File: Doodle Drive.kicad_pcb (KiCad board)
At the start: 2 copper layers, 99.1 x 99.1 mm, 52 parts, among them J1 USB_C_Receptacle, J2 PINHD_1x4_Male, J3 PINHD_1x4_Male, SW1 Push_Button, SW2 Push_Button, SW3 Push_Button, U1 STM32F401CEUx, U2 DRV8825PWP, U6 AP7343-30W5-7, Y1 32.768KHz ±20ppm 12.5pF, Y3 25MHZ 9PF

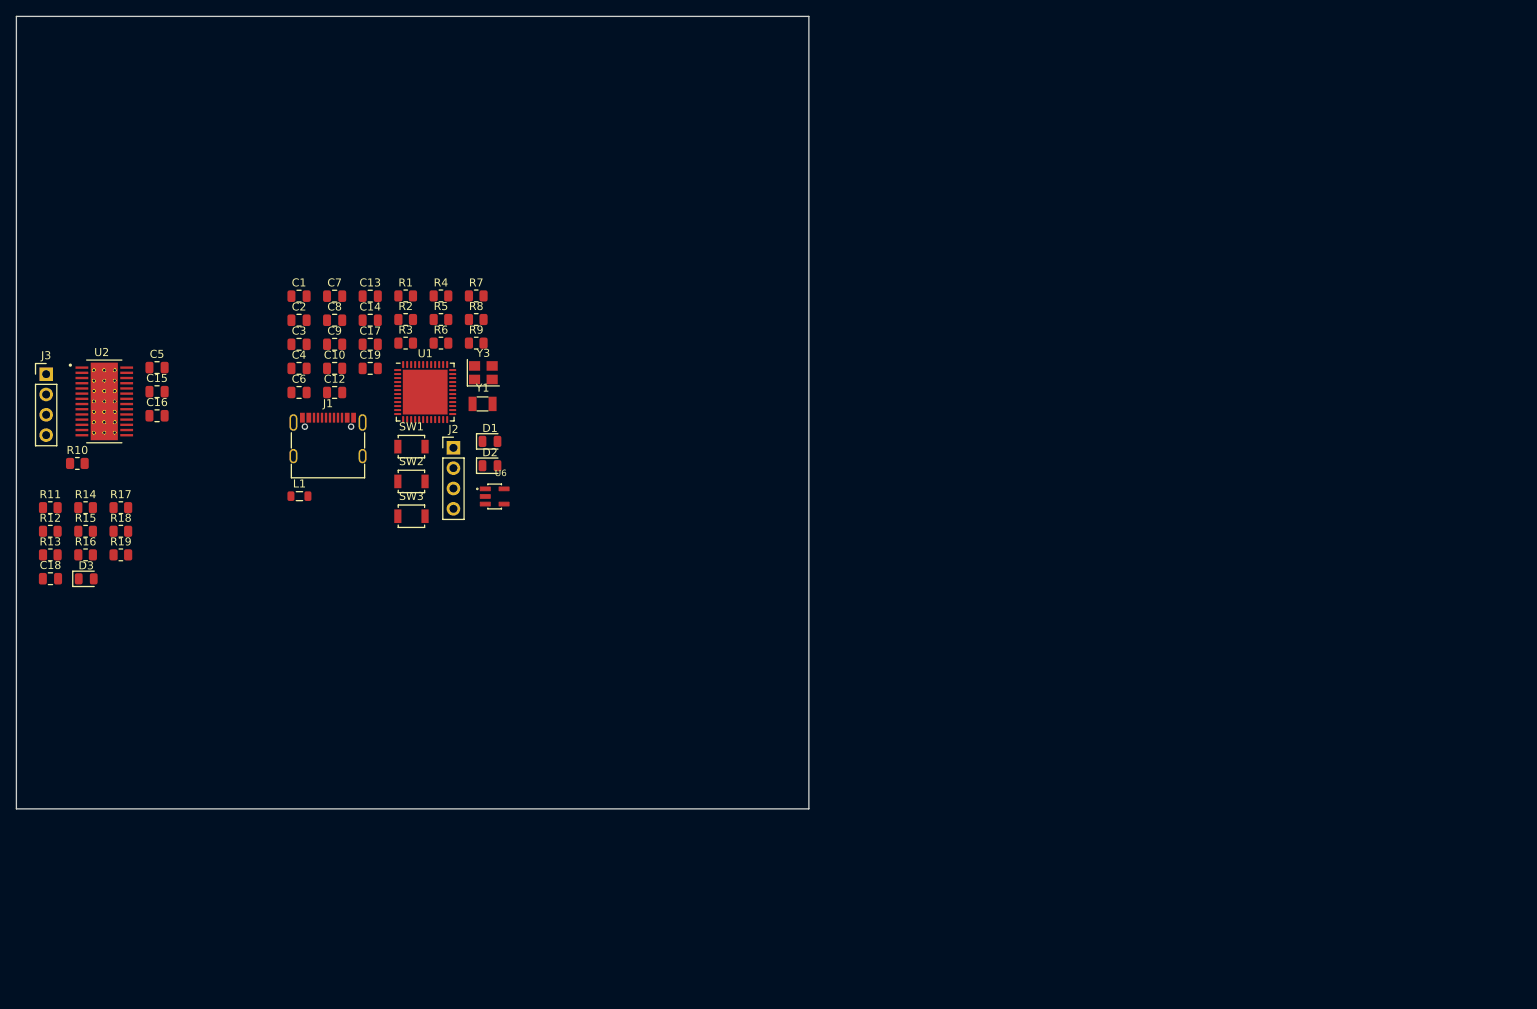
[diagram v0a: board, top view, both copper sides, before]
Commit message: fixed few errors, added test points
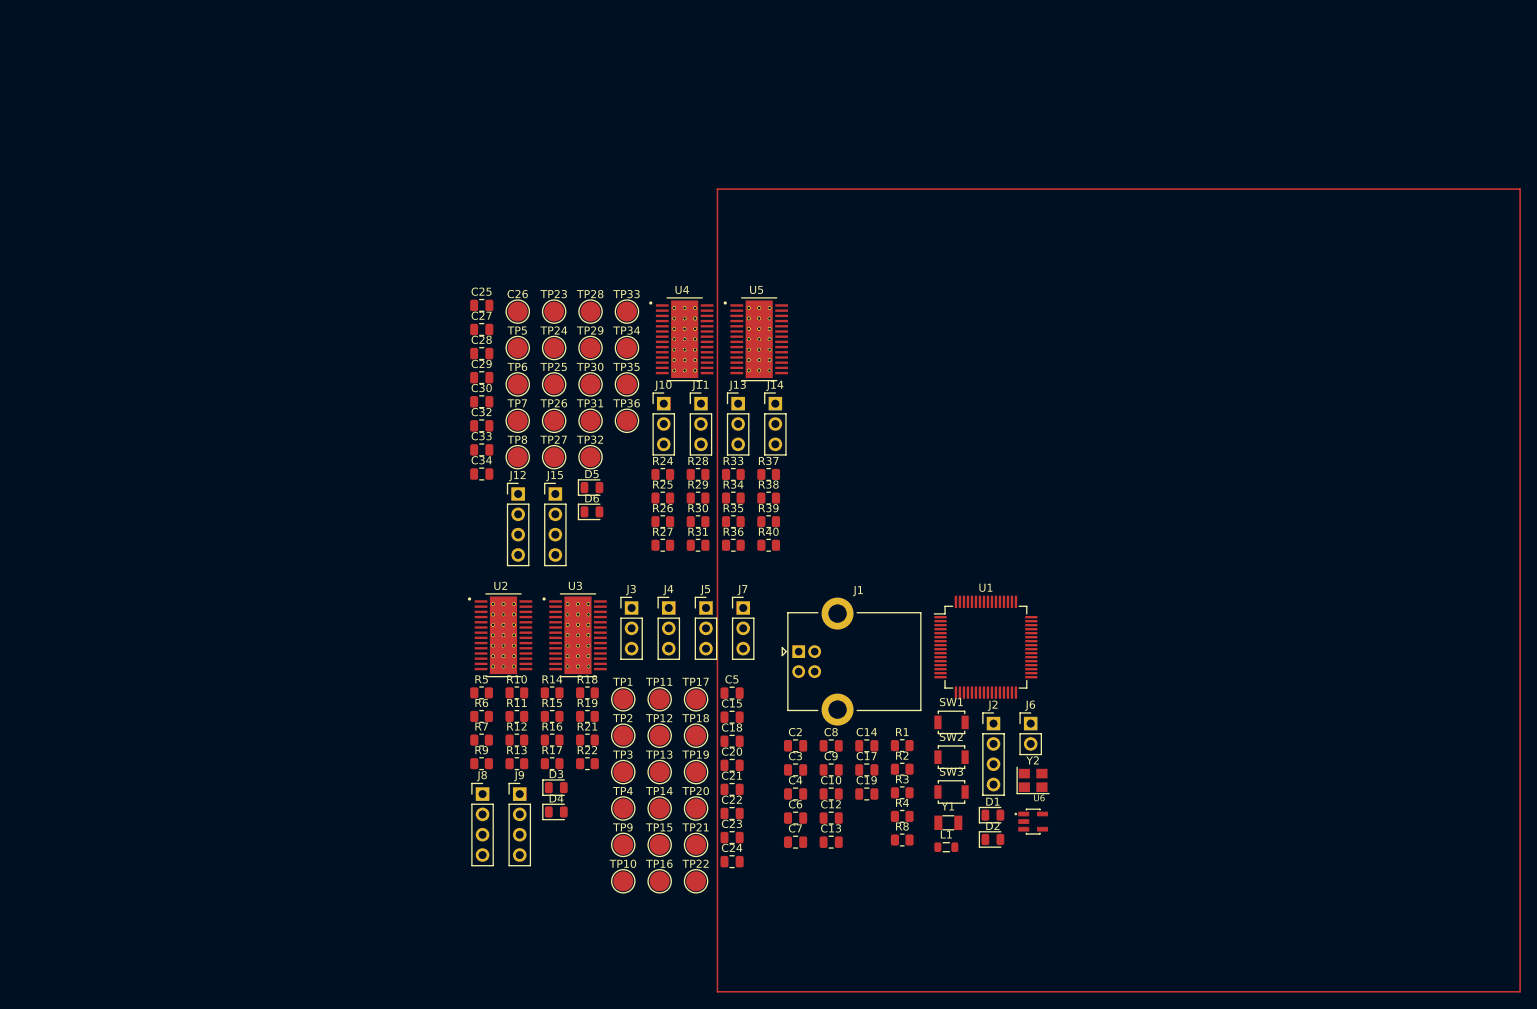
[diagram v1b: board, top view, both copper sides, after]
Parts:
- removed C1: 1uF, Capacitor_SMD:C_0805_2012Metric
- removed C16: Bulk Capacitance. 4.7uF?, Capacitor_SMD:C_0805_2012Metric
- removed Y3: 25MHZ 9PF, Crystal:Crystal_SMD_3225-4Pin_3.2x2.5mm
- added C20: 100nF 50V, Capacitor_SMD:C_0805_2012Metric, F.Cu at (135.2, 127.9)
- added C21: 100nF 50V, Capacitor_SMD:C_0805_2012Metric, F.Cu at (135.2, 130.9)
- added C22: Bulk Capacitance. 4.7uF?, Capacitor_SMD:C_0805_2012Metric, F.Cu at (135.2, 133.9)
- added C23: 100nF 50V, Capacitor_SMD:C_0805_2012Metric, F.Cu at (135.2, 136.9)
- added C24: 100nF 50V, Capacitor_SMD:C_0805_2012Metric, F.Cu at (135.2, 139.9)
- added C25: 10nF 50V, Capacitor_SMD:C_0805_2012Metric, F.Cu at (103.9, 70.4)
- added C26: 100nF 16V ceramic, TestPoint:TestPoint_Pad_D2.5mm, F.Cu at (108.4, 71.2)
- added C27: Bulk Capacitance. 4.7uF?, Capacitor_SMD:C_0805_2012Metric, F.Cu at (103.9, 73.4)
- added C28: 100nF 50V, Capacitor_SMD:C_0805_2012Metric, F.Cu at (103.9, 76.4)
- added C29: 100nF 50V, Capacitor_SMD:C_0805_2012Metric, F.Cu at (103.9, 79.5)
- added C30: 10nF 50V, Capacitor_SMD:C_0805_2012Metric, F.Cu at (103.9, 82.5)
- added C32: Bulk Capacitance. 4.7uF?, Capacitor_SMD:C_0805_2012Metric, F.Cu at (103.9, 85.5)
- added C33: 100nF 50V, Capacitor_SMD:C_0805_2012Metric, F.Cu at (103.9, 88.5)
- added C34: 100nF 50V, Capacitor_SMD:C_0805_2012Metric, F.Cu at (103.9, 91.5)
- added D4: LED_RED, LED_SMD:LED_0805_2012Metric, F.Cu at (113.2, 133.7)
- added D5: LED_RED, LED_SMD:LED_0805_2012Metric, F.Cu at (117.7, 93.2)
- added D6: LED_RED, LED_SMD:LED_0805_2012Metric, F.Cu at (117.7, 96.2)
- added J10: PINHD_1x3_Male, Connector_PinHeader_2.54mm:PinHeader_1x03_P2.54mm_Vertical, F.Cu at (126.6, 82.7)
- added J11: PINHD_1x3_Male, Connector_PinHeader_2.54mm:PinHeader_1x03_P2.54mm_Vertical, F.Cu at (131.3, 82.7)
- added J12: PINHD_1x4_Male, Connector_PinHeader_2.54mm:PinHeader_1x04_P2.54mm_Vertical, F.Cu at (108.4, 94.0)
- added J13: PINHD_1x3_Male, Connector_PinHeader_2.54mm:PinHeader_1x03_P2.54mm_Vertical, F.Cu at (135.9, 82.7)
- added J14: PINHD_1x3_Male, Connector_PinHeader_2.54mm:PinHeader_1x03_P2.54mm_Vertical, F.Cu at (140.6, 82.7)
- added J15: PINHD_1x4_Male, Connector_PinHeader_2.54mm:PinHeader_1x04_P2.54mm_Vertical, F.Cu at (113.1, 94.0)
- added J4: PINHD_1x3_Male, Connector_PinHeader_2.54mm:PinHeader_1x03_P2.54mm_Vertical, F.Cu at (127.3, 108.2)
- added J5: PINHD_1x3_Male, Connector_PinHeader_2.54mm:PinHeader_1x03_P2.54mm_Vertical, F.Cu at (131.9, 108.2)
- added J6: PINHD_1x2_Male, Connector_PinHeader_2.54mm:PinHeader_1x02_P2.54mm_Vertical, F.Cu at (172.5, 122.7)
- added J7: PINHD_1x3_Male, Connector_PinHeader_2.54mm:PinHeader_1x03_P2.54mm_Vertical, F.Cu at (136.6, 108.2)
- added J8: PINHD_1x4_Male, Connector_PinHeader_2.54mm:PinHeader_1x04_P2.54mm_Vertical, F.Cu at (104.0, 131.5)
- added J9: PINHD_1x4_Male, Connector_PinHeader_2.54mm:PinHeader_1x04_P2.54mm_Vertical, F.Cu at (108.6, 131.5)
- added R21: 10k, Resistor_SMD:R_0805_2012Metric, F.Cu at (117.1, 124.8)
- added R22: 5.1k, Resistor_SMD:R_0805_2012Metric, F.Cu at (117.1, 127.7)
- added R24: 0.1, Resistor_SMD:R_0805_2012Metric, F.Cu at (126.5, 91.5)
- added R25: 0.1, Resistor_SMD:R_0805_2012Metric, F.Cu at (126.5, 94.5)
- added R26: 1M, Resistor_SMD:R_0805_2012Metric, F.Cu at (126.5, 97.5)
- added R27: 1k, Resistor_SMD:R_0805_2012Metric, F.Cu at (126.5, 100.4)
- added R28: 300, Resistor_SMD:R_0805_2012Metric, F.Cu at (130.9, 91.5)
- added R29: 300, Resistor_SMD:R_0805_2012Metric, F.Cu at (130.9, 94.5)
- added R30: 10k, Resistor_SMD:R_0805_2012Metric, F.Cu at (130.9, 97.5)
- added R31: 5.1k, Resistor_SMD:R_0805_2012Metric, F.Cu at (130.9, 100.4)
- added R33: 0.1, Resistor_SMD:R_0805_2012Metric, F.Cu at (135.3, 91.5)
- added R34: 0.1, Resistor_SMD:R_0805_2012Metric, F.Cu at (135.3, 94.5)
- added R35: 1M, Resistor_SMD:R_0805_2012Metric, F.Cu at (135.3, 97.5)
- added R36: 1k, Resistor_SMD:R_0805_2012Metric, F.Cu at (135.3, 100.4)
- added R37: 300, Resistor_SMD:R_0805_2012Metric, F.Cu at (139.7, 91.5)
- added R38: 300, Resistor_SMD:R_0805_2012Metric, F.Cu at (139.7, 94.5)
- added R39: 10k, Resistor_SMD:R_0805_2012Metric, F.Cu at (139.7, 97.5)
- added R40: 5.1k, Resistor_SMD:R_0805_2012Metric, F.Cu at (139.7, 100.4)
- added TP1: TestPoint, TestPoint:TestPoint_Pad_D2.5mm, F.Cu at (121.6, 119.7)
- added TP10: TestPoint, TestPoint:TestPoint_Pad_D2.5mm, F.Cu at (121.6, 142.4)
- added TP11: TestPoint, TestPoint:TestPoint_Pad_D2.5mm, F.Cu at (126.1, 119.7)
- added TP12: TestPoint, TestPoint:TestPoint_Pad_D2.5mm, F.Cu at (126.1, 124.2)
- added TP13: TestPoint, TestPoint:TestPoint_Pad_D2.5mm, F.Cu at (126.1, 128.8)
- added TP14: TestPoint, TestPoint:TestPoint_Pad_D2.5mm, F.Cu at (126.1, 133.3)
- added TP15: TestPoint, TestPoint:TestPoint_Pad_D2.5mm, F.Cu at (126.1, 137.8)
- added TP16: TestPoint, TestPoint:TestPoint_Pad_D2.5mm, F.Cu at (126.1, 142.4)
- added TP17: TestPoint, TestPoint:TestPoint_Pad_D2.5mm, F.Cu at (130.7, 119.7)
- added TP18: TestPoint, TestPoint:TestPoint_Pad_D2.5mm, F.Cu at (130.7, 124.2)
- added TP19: TestPoint, TestPoint:TestPoint_Pad_D2.5mm, F.Cu at (130.7, 128.8)
- added TP2: TestPoint, TestPoint:TestPoint_Pad_D2.5mm, F.Cu at (121.6, 124.2)
- added TP20: TestPoint, TestPoint:TestPoint_Pad_D2.5mm, F.Cu at (130.7, 133.3)
- added TP21: TestPoint, TestPoint:TestPoint_Pad_D2.5mm, F.Cu at (130.7, 137.8)
- added TP22: TestPoint, TestPoint:TestPoint_Pad_D2.5mm, F.Cu at (130.7, 142.4)
- added TP23: TestPoint, TestPoint:TestPoint_Pad_D2.5mm, F.Cu at (112.9, 71.2)
- added TP24: TestPoint, TestPoint:TestPoint_Pad_D2.5mm, F.Cu at (112.9, 75.7)
- added TP25: TestPoint, TestPoint:TestPoint_Pad_D2.5mm, F.Cu at (112.9, 80.3)
- added TP26: TestPoint, TestPoint:TestPoint_Pad_D2.5mm, F.Cu at (112.9, 84.8)
- added TP27: TestPoint, TestPoint:TestPoint_Pad_D2.5mm, F.Cu at (112.9, 89.4)
- added TP28: TestPoint, TestPoint:TestPoint_Pad_D2.5mm, F.Cu at (117.5, 71.2)
- added TP29: TestPoint, TestPoint:TestPoint_Pad_D2.5mm, F.Cu at (117.5, 75.7)
- added TP3: TestPoint, TestPoint:TestPoint_Pad_D2.5mm, F.Cu at (121.6, 128.8)
- added TP30: TestPoint, TestPoint:TestPoint_Pad_D2.5mm, F.Cu at (117.5, 80.3)
- added TP31: TestPoint, TestPoint:TestPoint_Pad_D2.5mm, F.Cu at (117.5, 84.8)
- added TP32: TestPoint, TestPoint:TestPoint_Pad_D2.5mm, F.Cu at (117.5, 89.4)
- added TP33: TestPoint, TestPoint:TestPoint_Pad_D2.5mm, F.Cu at (122.0, 71.2)
- added TP34: TestPoint, TestPoint:TestPoint_Pad_D2.5mm, F.Cu at (122.0, 75.7)
- added TP35: TestPoint, TestPoint:TestPoint_Pad_D2.5mm, F.Cu at (122.0, 80.3)
- added TP36: TestPoint, TestPoint:TestPoint_Pad_D2.5mm, F.Cu at (122.0, 84.8)
- added TP4: TestPoint, TestPoint:TestPoint_Pad_D2.5mm, F.Cu at (121.6, 133.3)
- added TP5: TestPoint, TestPoint:TestPoint_Pad_D2.5mm, F.Cu at (108.4, 75.7)
- added TP6: TestPoint, TestPoint:TestPoint_Pad_D2.5mm, F.Cu at (108.4, 80.3)
- added TP7: TestPoint, TestPoint:TestPoint_Pad_D2.5mm, F.Cu at (108.4, 84.8)
- added TP8: TestPoint, TestPoint:TestPoint_Pad_D2.5mm, F.Cu at (108.4, 89.4)
- added TP9: TestPoint, TestPoint:TestPoint_Pad_D2.5mm, F.Cu at (121.6, 137.8)
- added U3: DRV8825PWP, DRV8825PWP:IC_TPS61196PWPRQ1, F.Cu at (115.9, 111.6)
- added U4: DRV8825PWP, DRV8825PWP:IC_TPS61196PWPRQ1, F.Cu at (129.3, 74.6)
- added U5: DRV8825PWP, DRV8825PWP:IC_TPS61196PWPRQ1, F.Cu at (138.6, 74.6)
- added Y2: 25MHZ 9PF, Crystal:Crystal_SMD_3225-4Pin_3.2x2.5mm, F.Cu at (172.8, 129.8)
- C15: value 100nF 50V -> 10nF 50V
- C18: value 100nF 50V -> Bulk Capacitance. 4.7uF?
- C7: value 12pF -> 15pF
- C9: value 15pF -> 12pF
- J1: value USB_C_Receptacle -> USB_B; footprint Connector_USB:USB_C_Receptacle_G-Switch_GT-USB-7010ASV -> Connector_USB:USB_B_Lumberg_2411_02_Horizontal
- J3: value PINHD_1x4_Male -> PINHD_1x3_Male; footprint Connector_PinHeader_2.54mm:PinHeader_1x04_P2.54mm_Vertical -> Connector_PinHeader_2.54mm:PinHeader_1x03_P2.54mm_Vertical
- R10: value 10k -> 300
- R11: value 1k -> 300
- R12, R13: value 300 -> 0.1
- R15: value 10k -> 0.1
- R17: value 0.1 -> 1M
- R18: value 1.5k -> 10k
- R5: value 5.1k -> 1k
- R6: value 10 -> 1k
- R7: value 10 -> 300
- R9: value 5.1k -> 300
- U1: value STM32F401CEUx -> STM32F411RETx; footprint Package_DFN_QFN:QFN-48-1EP_7x7mm_P0.5mm_EP5.6x5.6mm -> Package_QFP:LQFP-64_10x10mm_P0.5mm
- moved L1 92.0 mm to (162.0, 138.1)
- moved C7 89.3 mm to (143.1, 137.5)
- moved C13 89.3 mm to (147.6, 137.5)
- moved C18 87.6 mm to (135.2, 124.9)
- moved R4 86.9 mm to (156.4, 134.3)
- moved R8 84.1 mm to (156.4, 137.2)
- moved R1 83.7 mm to (156.4, 125.4)
- moved R3 83.7 mm to (156.4, 131.3)
- moved R2 83.7 mm to (156.4, 128.4)
- moved C15 82.6 mm to (135.2, 121.9)
- moved C5 82.6 mm to (135.2, 118.9)
- moved C14 81.7 mm to (152.0, 125.5)
- moved C17 81.7 mm to (152.0, 128.5)
- moved C19 81.7 mm to (152.0, 131.5)
- moved C2 81.7 mm to (143.1, 125.5)
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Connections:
- net PA15 renamed PC7
- net PB11 renamed PC5
- net PB3 renamed PC8
- net PB4 renamed PC9
- C10 pad 1: Net-(U1-PC15) -> PC13
- C15 pad 1: VM -> Net-(U3-CP2)
- C15 pad 2: GND -> Net-(U3-CP1)
- C18 pad 1: Net-(U2-VMB) -> GND
- C18 pad 2: GND -> VM
- C5 pad 1: Net-(U2-CP1) -> Net-(U2-CP2)
- C5 pad 2: Net-(U2-CP2) -> Net-(U2-CP1)
- C6 pad 2: Net-(U1-PH0) -> PH1
- C7 pad 2: Net-(U1-PH1) -> PC14
- C9 pad 2: Net-(U1-PC14) -> PH0
- D3 pad 2: Net-(D3-A) -> NFAULT2
- J3 pad 1: Net-(U2-AOUT1) -> Net-(J3-Pad1)
- J3 pad 2: Net-(U2-AOUT2) -> Net-(J3-Pad2)
- J3 pad 3: Net-(U2-BOUT1) -> Net-(J3-Pad3)
- R10 pad 1: NFAULT -> Net-(R10-Pad1)
- R10 pad 2: NSLEEP -> Net-(J5-Pad1)
- R11 pad 1: 1V25 -> Net-(J7-Pad3)
- R11 pad 2: +3V3 -> Net-(R10-Pad1)
- R12 pad 1: Net-(R12-Pad1) -> Net-(U2-ISENA)
- R12 pad 2: 1V25 -> GND
- R13 pad 2: Net-(R12-Pad1) -> Net-(U2-ISENB)
- R15 pad 1: NHOME -> Net-(U3-ISENA)
- R15 pad 2: +3V3 -> GND
- R16 pad 2: Net-(U2-ISENB) -> Net-(U3-ISENB)
- R17 pad 1: GND -> Net-(U3-VCP)
- R17 pad 2: Net-(U2-ISENA) -> VM
- R18 pad 1: Net-(U2-NFAULT) -> NSLEEP2
- R18 pad 2: NFAULT -> NHOME2
- R19 pad 1: Net-(D3-A) -> NFAULT2
- R19 pad 2: NFAULT -> Net-(U2-NFAULT)
- R5 pad 1: GND -> Net-(J3-Pad2)
- R5 pad 2: Net-(J1-CC1) -> +3V3
- R6 pad 1: PA11 -> Net-(J5-Pad2)
- R6 pad 2: Net-(J1-D--PadA7) -> +3V3
- R7 pad 1: Net-(J1-D+-PadA6) -> Net-(R7-Pad1)
- R7 pad 2: PA12 -> Net-(J3-Pad1)
- R9 pad 1: Net-(J1-CC2) -> Net-(J4-Pad3)
- R9 pad 2: GND -> Net-(R7-Pad1)
- U1 pad 10: PA0 -> NSLEEP4
- U1 pad 11: PA1 -> NRESET4
- U1 pad 12: PA2 -> GND
- U1 pad 13: PA3 -> VREF+
- U1 pad 14: PA4 -> PA0
- U1 pad 15: PA5 -> DIR1
- U1 pad 16: PA6 -> PA2
- U1 pad 17: PA7 -> NENBL1
- U1 pad 18: PB0 -> GND
- U1 pad 19: PB1 -> +3V3
- U1 pad 20: PB2 -> NHOME1
- U1 pad 21: PB10 -> NFAULT1
- U1 pad 22: Net-(U1-VCAP1) -> NSLEEP1
- U1 pad 23: GND -> NRESET1
- U1 pad 24: +3V3 -> PC4
- U1 pad 26: PB12 -> NFAULT2
- U1 pad 27: PB13 -> NSLEEP2
- U1 pad 28: PB14 -> PB2
- U1 pad 29: PA8 -> NSLEEP3
- U1 pad 3: Net-(U1-PC14) -> PC14
- U1 pad 30: PA9 -> Net-(U1-VCAP1)
- U1 pad 31: PA10 -> GND
- U1 pad 32: PA11 -> +3V3
- U1 pad 33: PA12 -> NRESET3
- U1 pad 34: PA13 -> DIR4
- U1 pad 35: GND -> PB14
- U1 pad 36: +3V3 -> NENBL4
- U1 pad 37: PA14 -> PC6
- U1 pad 4: Net-(U1-PC15) -> PC15
- U1 pad 41: PB5 -> DIR2
- U1 pad 42: PB6 -> PA9
- U1 pad 43: PB7 -> NENBL2
- U1 pad 44: BOOT0 -> PA11
- U1 pad 45: PB8 -> PA12
- U1 pad 46: PB9 -> PA13
- U1 pad 49: GND -> PA14
- U1 pad 5: Net-(U1-PH0) -> PH0
- U1 pad 6: Net-(U1-PH1) -> PH1
- U1 pad 8: GND -> NHOME4
- U1 pad 9: VREF+ -> NFAULT4
- U2 pad 12: 1V25 -> VREF2
- U2 pad 13: 1V25 -> VREF2
- U2 pad 16: NRESET -> NRESET2
- U2 pad 17: NSLEEP -> NSLEEP2
- U2 pad 20: DIR1 -> DIR2
- U2 pad 21: NENBL -> NENBL2
- U2 pad 22: STEP -> PA9
- U2 pad 27: NHOME -> NHOME2
- Y1 pad 1: Net-(U1-PC15) -> PC13
- Y1 pad 2: Net-(U1-PC14) -> PC14
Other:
- board outline removed

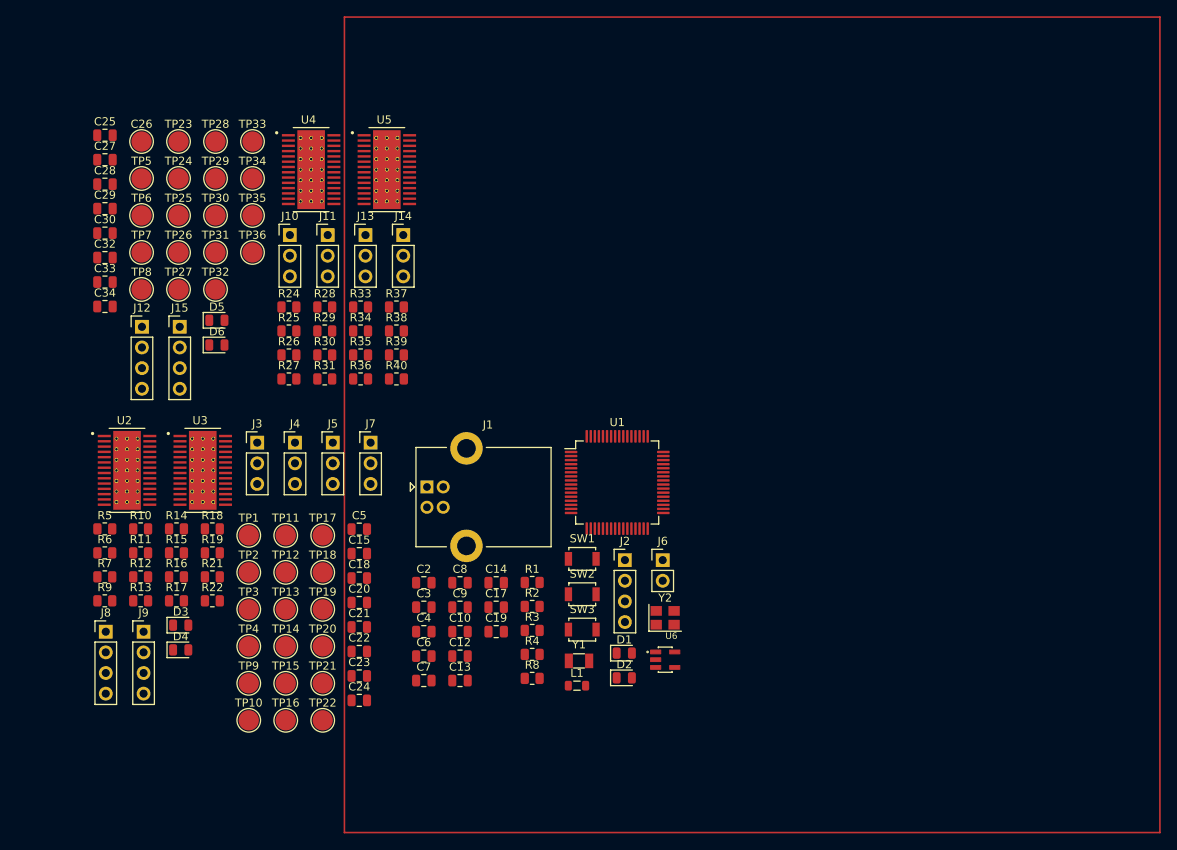
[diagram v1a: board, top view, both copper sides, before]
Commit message: add CP2102 USB to UART chip
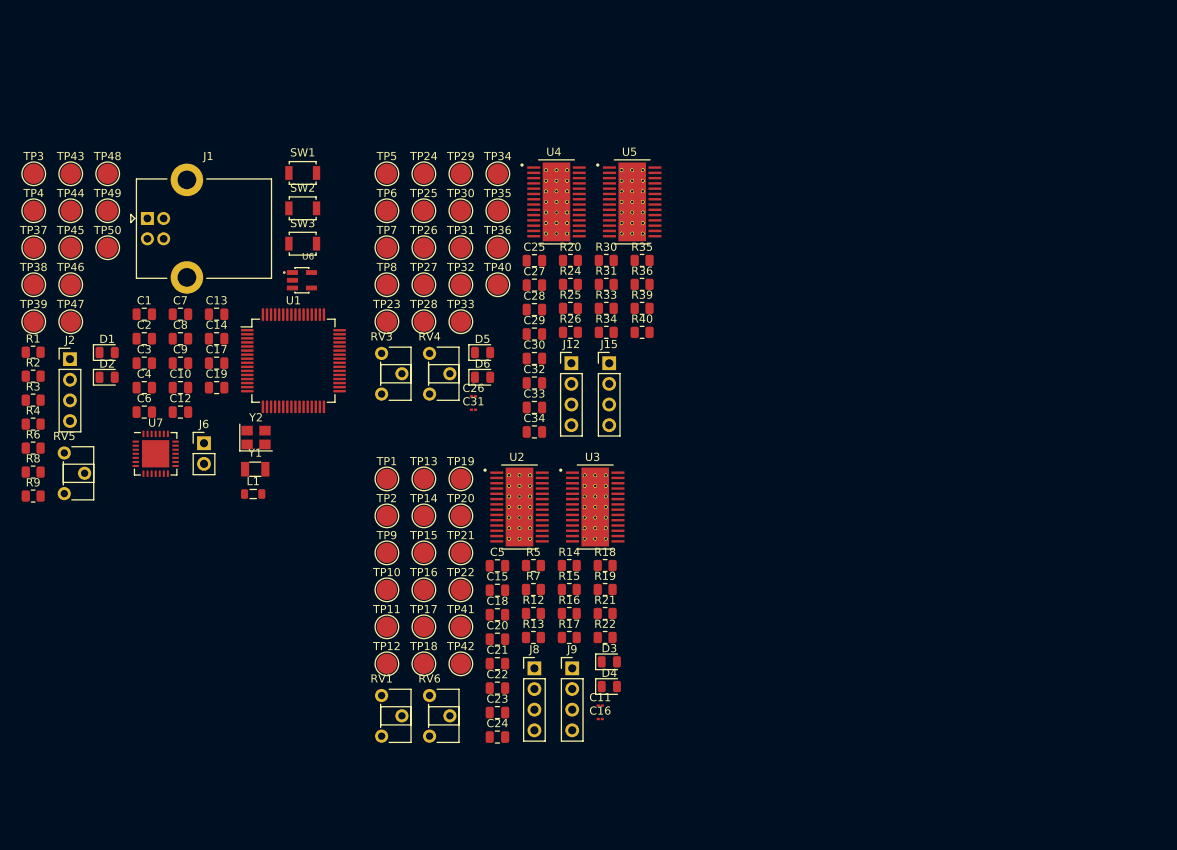
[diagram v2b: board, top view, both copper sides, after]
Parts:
- removed J10, J11, J13, J14, J3, J4, J5, J7: PINHD_1x3_Male, Connector_PinHeader_2.54mm:PinHeader_1x03_P2.54mm_Vertical
- removed R10, R11, R28, R29, R37, R38: 300, Resistor_SMD:R_0805_2012Metric
- removed R27: 1k, Resistor_SMD:R_0805_2012Metric
- added C1: 1uF, Capacitor_SMD:C_0805_2012Metric, F.Cu at (108.7, 92.4)
- added C11: 100nF 16V ceramic, Capacitor_SMD:C_01005_0402Metric, F.Cu at (164.8, 140.6)
- added C16: 100nF 16V ceramic, Capacitor_SMD:C_01005_0402Metric, F.Cu at (164.8, 142.2)
- added C31: 100nF 16V ceramic, Capacitor_SMD:C_01005_0402Metric, F.Cu at (149.2, 104.2)
- added R20: 1k, Resistor_SMD:R_0805_2012Metric, F.Cu at (161.2, 85.8)
- added RV1: R_Potentiometer, Potentiometer_THT:Potentiometer_ACP_CA6-H2,5_Horizontal, F.Cu at (137.9, 139.3)
- added RV3: R_Potentiometer, Potentiometer_THT:Potentiometer_ACP_CA6-H2,5_Horizontal, F.Cu at (137.9, 97.3)
- added RV4: R_Potentiometer, Potentiometer_THT:Potentiometer_ACP_CA6-H2,5_Horizontal, F.Cu at (143.8, 97.3)
- added RV5: R_Potentiometer, Potentiometer_THT:Potentiometer_ACP_CA6-H2,5_Horizontal, F.Cu at (98.9, 109.5)
- added RV6: R_Potentiometer, Potentiometer_THT:Potentiometer_ACP_CA6-H2,5_Horizontal, F.Cu at (143.8, 139.3)
- added TP37: TestPoint, TestPoint:TestPoint_Pad_D2.5mm, F.Cu at (95.1, 84.3)
- added TP38: TestPoint, TestPoint:TestPoint_Pad_D2.5mm, F.Cu at (95.1, 88.8)
- added TP39: TestPoint, TestPoint:TestPoint_Pad_D2.5mm, F.Cu at (95.1, 93.4)
- added TP40: TestPoint, TestPoint:TestPoint_Pad_D2.5mm, F.Cu at (152.2, 88.8)
- added TP41: TestPoint, TestPoint:TestPoint_Pad_D2.5mm, F.Cu at (147.7, 130.9)
- added TP42: TestPoint, TestPoint:TestPoint_Pad_D2.5mm, F.Cu at (147.7, 135.4)
- added TP43: TestPoint, TestPoint:TestPoint_Pad_D2.5mm, F.Cu at (99.7, 75.2)
- added TP44: TestPoint, TestPoint:TestPoint_Pad_D2.5mm, F.Cu at (99.7, 79.7)
- added TP45: TestPoint, TestPoint:TestPoint_Pad_D2.5mm, F.Cu at (99.7, 84.3)
- added TP46: TestPoint, TestPoint:TestPoint_Pad_D2.5mm, F.Cu at (99.7, 88.8)
- added TP47: TestPoint, TestPoint:TestPoint_Pad_D2.5mm, F.Cu at (99.7, 93.4)
- added TP48: TestPoint, TestPoint:TestPoint_Pad_D2.5mm, F.Cu at (104.2, 75.2)
- added TP49: TestPoint, TestPoint:TestPoint_Pad_D2.5mm, F.Cu at (104.2, 79.7)
- added TP50: TestPoint, TestPoint:TestPoint_Pad_D2.5mm, F.Cu at (104.2, 84.3)
- added U7: CP2102N-Axx-xQFN28, Package_DFN_QFN:QFN-28-1EP_5x5mm_P0.5mm_EP3.35x3.35mm, F.Cu at (110.1, 109.6)
- C26: footprint TestPoint:TestPoint_Pad_D2.5mm -> Capacitor_SMD:C_01005_0402Metric
- R6: value 1k -> 8.2k
- R7: value 300 -> 1k
- R9: value 300 -> 11k
- moved D2 73.6 mm to (104.2, 100.2)
- moved D1 73.6 mm to (104.2, 97.2)
- moved J2 72.6 mm to (99.6, 98.0)
- moved R1 67.6 mm to (95.1, 97.1)
- moved R2 67.6 mm to (95.1, 100.1)
- moved R3 67.6 mm to (95.1, 103.0)
- moved R4 67.6 mm to (95.1, 106.0)
- moved R8 66.4 mm to (95.1, 111.9)
- moved U6 64.6 mm to (128.1, 88.3)
- moved TP4 59.8 mm to (95.1, 79.7)
- moved TP3 59.8 mm to (95.1, 75.2)
- moved SW1 58.6 mm to (128.2, 75.1)
- moved SW2 58.6 mm to (128.2, 79.4)
- moved SW3 58.6 mm to (128.2, 83.8)
- moved J6 58.2 mm to (116.1, 108.3)
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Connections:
- net PC14 renamed NSUSPEND
- net VREF2 renamed Net-(U2-AVREF)
- net VREF3 renamed Net-(U4-AVREF)
- net VREF4 renamed Net-(U5-AVREF)
- C21 pad 1: Net-(U2-VMB) -> VM
- C24 pad 1: Net-(U3-VMB) -> VM
- C29 pad 1: Net-(U4-VMB) -> VM
- C34 pad 1: Net-(U5-VMB) -> VM
- J1 pad 2: PA12 -> Net-(J1-D-)
- J1 pad 3: PA11 -> Net-(J1-D+)
- J6 pad 1: PB6 -> Net-(J6-Pad1)
- R6 pad 1: Net-(J5-Pad2) -> Net-(U7-~{RST})
- R6 pad 2: +3V3 -> Net-(U7-VDD)
- R7 pad 2: Net-(J3-Pad1) -> +3V3
- R9 pad 1: Net-(J4-Pad3) -> Net-(U7-~{RST})
- R9 pad 2: Net-(R7-Pad1) -> Net-(U7-VDD)
- TP3 pad 1: Net-(J5-Pad2) -> +5V
- TP4 pad 1: VREF1 -> PC7
- U1 pad 24: PC4 -> NRTS
- U1 pad 25: PC5 -> NCTS
- U1 pad 39: PC8 -> NDSR
- U1 pad 40: PC9 -> NDTR
- U1 pad 51: PC10 -> NDCD
- U1 pad 52: PC11 -> NRI
- U2 pad 11: Net-(U2-VMB) -> VM
- U3 pad 11: Net-(U3-VMB) -> VM
- U3 pad 12: VREF1 -> Net-(U3-AVREF)
- U3 pad 13: VREF1 -> Net-(U3-AVREF)
- U4 pad 11: Net-(U4-VMB) -> VM
- U5 pad 11: Net-(U5-VMB) -> VM

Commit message: deleted unnecessary testpoints
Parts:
- removed TP2, TP41, TP5, TP7: TestPoint, TestPoint:TestPoint_Pad_D2.5mm
- moved C11 208.0 mm to (-37.8, 93.7)
- moved C16 208.0 mm to (-37.8, 95.4)
- moved D3 208.0 mm to (-36.7, 88.4)
- moved D4 208.0 mm to (-36.7, 91.4)
- moved C15 197.9 mm to (-36.7, 67.3)
- moved C18 197.9 mm to (-36.7, 70.3)
- moved C21 197.9 mm to (-36.7, 76.3)
- moved C22 197.9 mm to (-36.7, 79.3)
- moved C23 197.9 mm to (-36.7, 82.3)
- moved C24 197.9 mm to (-36.7, 85.3)
- moved C5 197.9 mm to (-36.7, 64.3)
- moved C20 197.9 mm to (-36.7, 73.3)
- moved U3 190.5 mm to (-20.3, 68.5)
- moved U2 190.5 mm to (-29.6, 68.5)
- moved TP24 184.4 mm to (-36.7, 116.2)
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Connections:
- C7 pad 2: NSUSPEND -> PC14
- U1 pad 3: NSUSPEND -> PC14
- U1 pad 54: PD2 -> NSUSPEND
- Y1 pad 2: NSUSPEND -> PC14

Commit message: started work on pcb
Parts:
- moved RV5 228.7 mm to (151.1, 76.3)
- moved J12 208.1 mm to (188.0, 100.3)
- moved RV3 205.0 mm to (166.4, 106.7)
- moved TP3 204.1 mm to (113.0, 130.8)
- moved U3 199.5 mm to (179.1, 59.7)
- moved U4 198.2 mm to (177.8, 104.1), turned to 180 degrees
- moved J9 184.8 mm to (170.2, 44.5)
- moved U1 180.3 mm to (132.1, 83.8)
- moved RV6 174.7 mm to (166.3, 62.3)
- moved J15 172.7 mm to (158.8, 123.2)
- moved RV4 171.2 mm to (139.7, 125.8)
- moved U5 162.3 mm to (149.9, 127.0), turned to 180 degrees
- moved U2 156.1 mm to (125.7, 52.1)
- moved J8 140.4 mm to (118.1, 40.6)
- moved RV1 129.1 mm to (114.3, 53.4)
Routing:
- added copper zone on F.Cu, net GND
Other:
- board outline added: 97.8 x 99.1 mm
